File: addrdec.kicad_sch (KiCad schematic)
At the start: 4 parts, among them U10 74LS138, U11 74HCT00, U24 74LS32, U9 74LS27

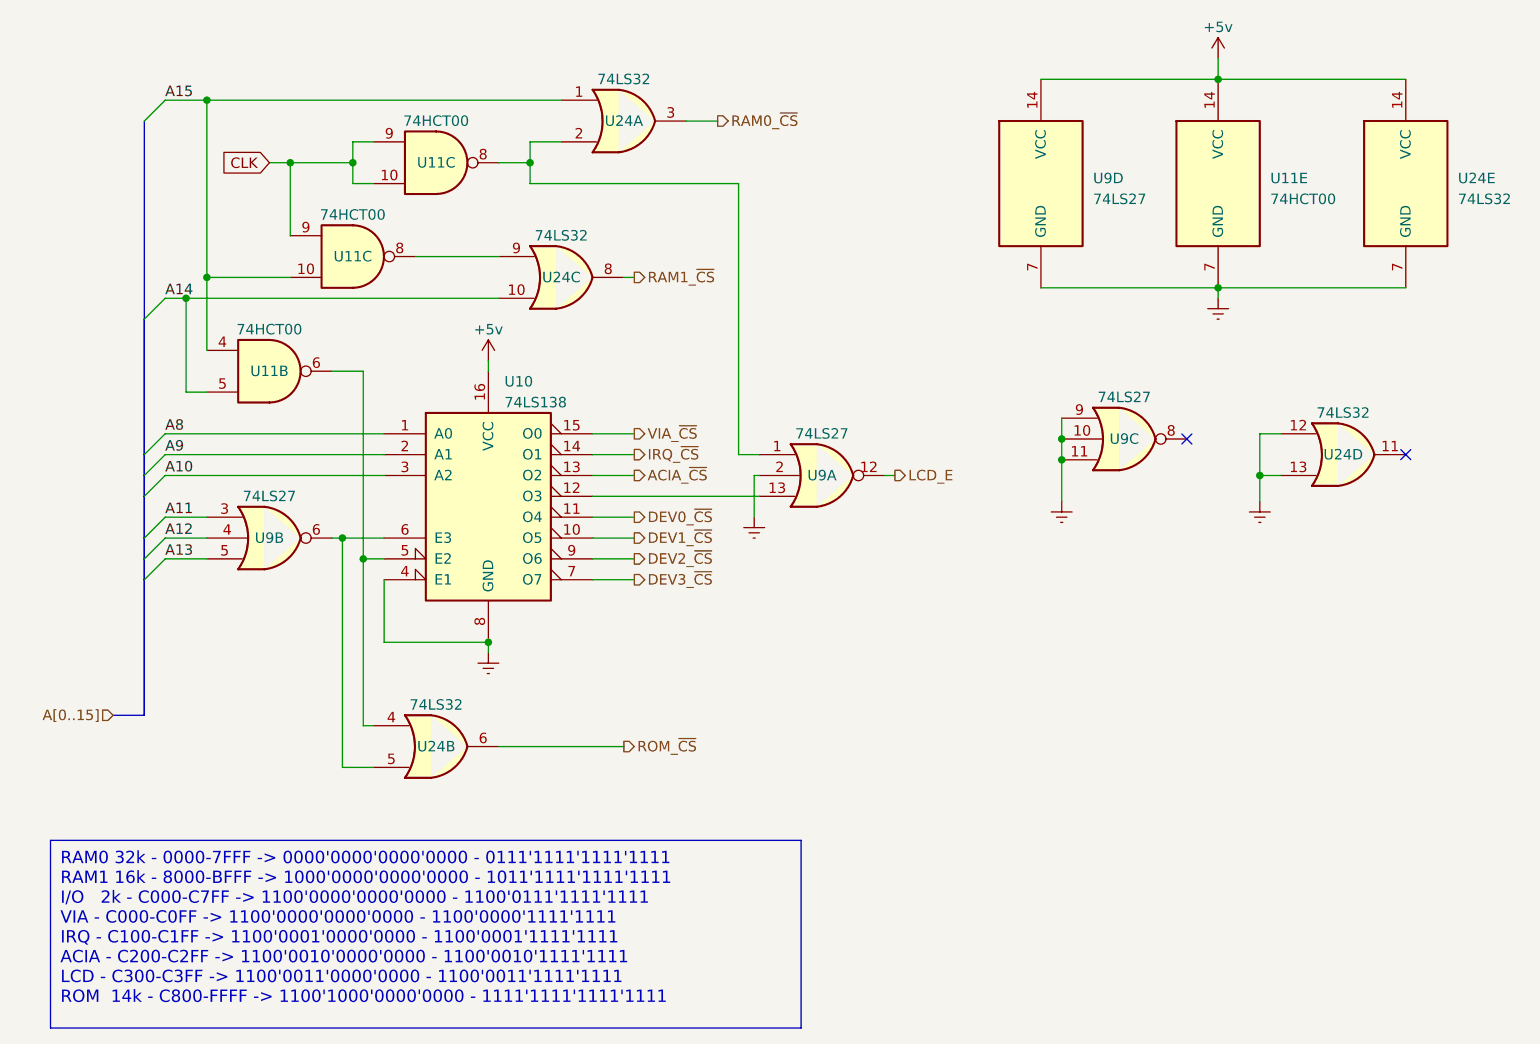
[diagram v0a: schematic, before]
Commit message: fix addrdec design bug, use ca65/cmake instead of vasm/make
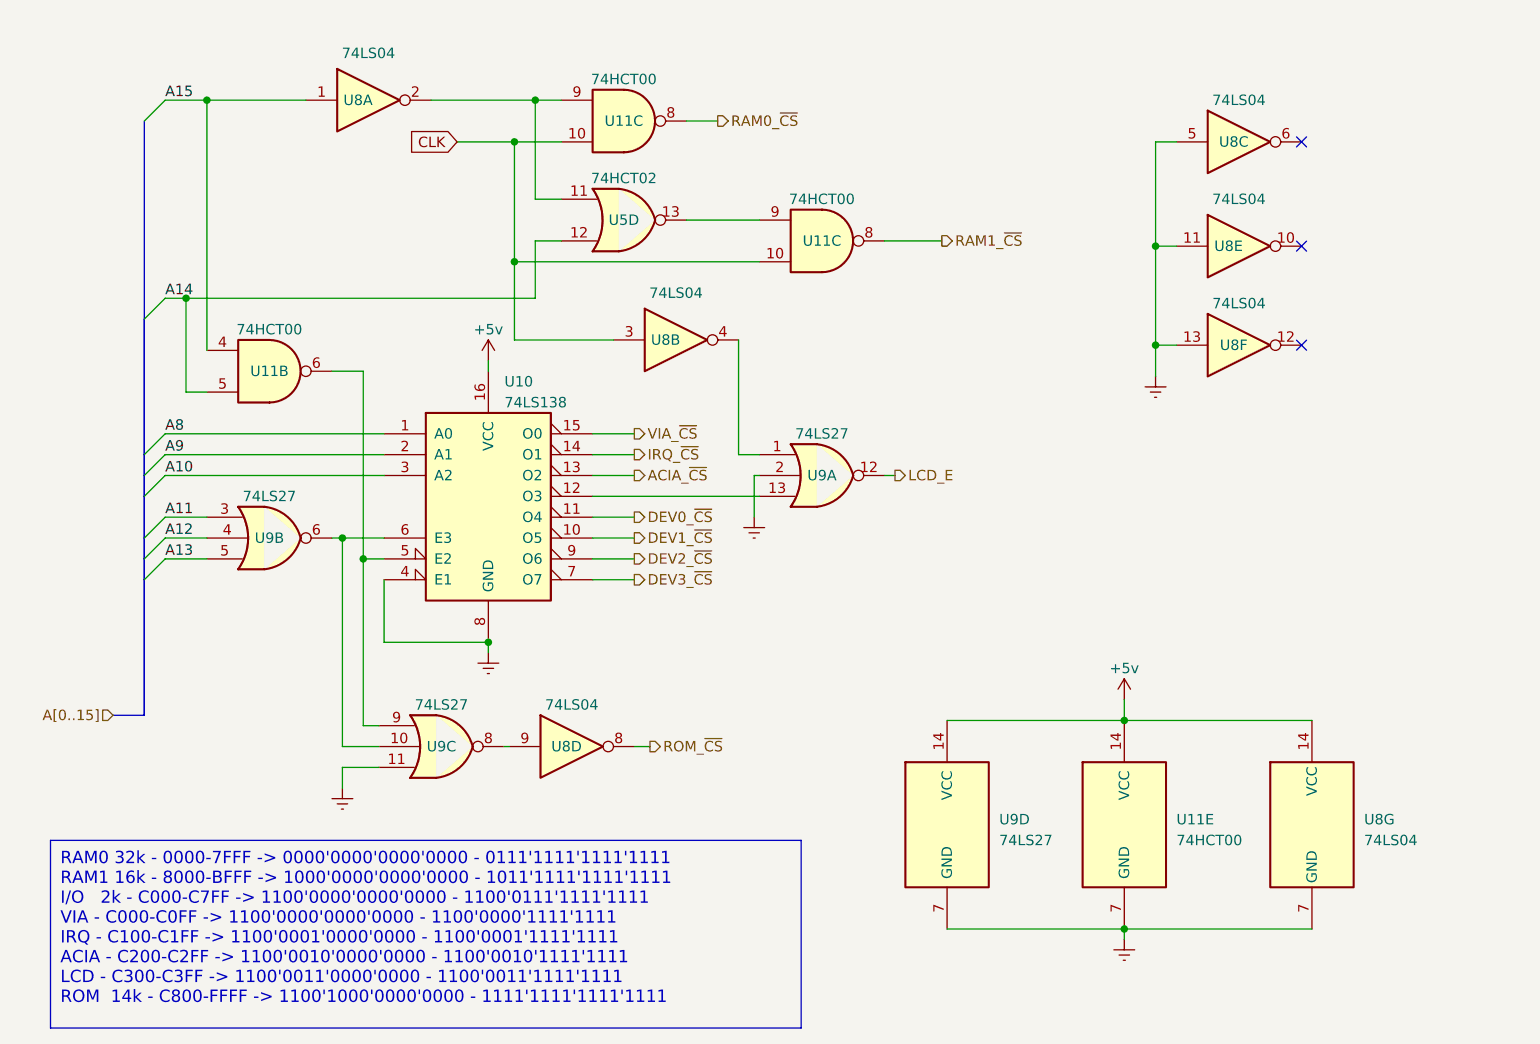
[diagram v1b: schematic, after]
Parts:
- removed U24: 74LS32, symbol 74xx:74LS32
- added U5: 74HCT02, symbol 74xx:74HCT02
- added U8: 74LS04, symbol 74xx:74LS04
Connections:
- net A14: now also U5.12
- net A15: now also U8.1; no longer U11.10
- net CLK: now also U11.10, U8.3; no longer U11.9, U11.9
- net Earth: now also U8.11, U8.13, U8.5, U8.7 (GND); no longer U9.10, U9.9
- net RAM0_~{CS}: now also U11.8
- net RAM1_~{CS}: now also U11.8
- net ROM_~{CS}: now also U8.8
- net VCC: now also U8.14 (VCC)
- net at U10.6 (E3), U9.6: now also U9.10
- net at U9.8: now also U8.9
- net at U9.1: now also U8.4; no longer U11.8
- net at U10.5 (E2), U11.6: now also U9.9
- new net: U11.9, U5.11, U8.2
- new net: U11.9, U5.13
- no-connect marks 2 -> 3
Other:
- moved on the sheet: U11C, U11E, U9C, U9D

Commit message: add address decoding timings
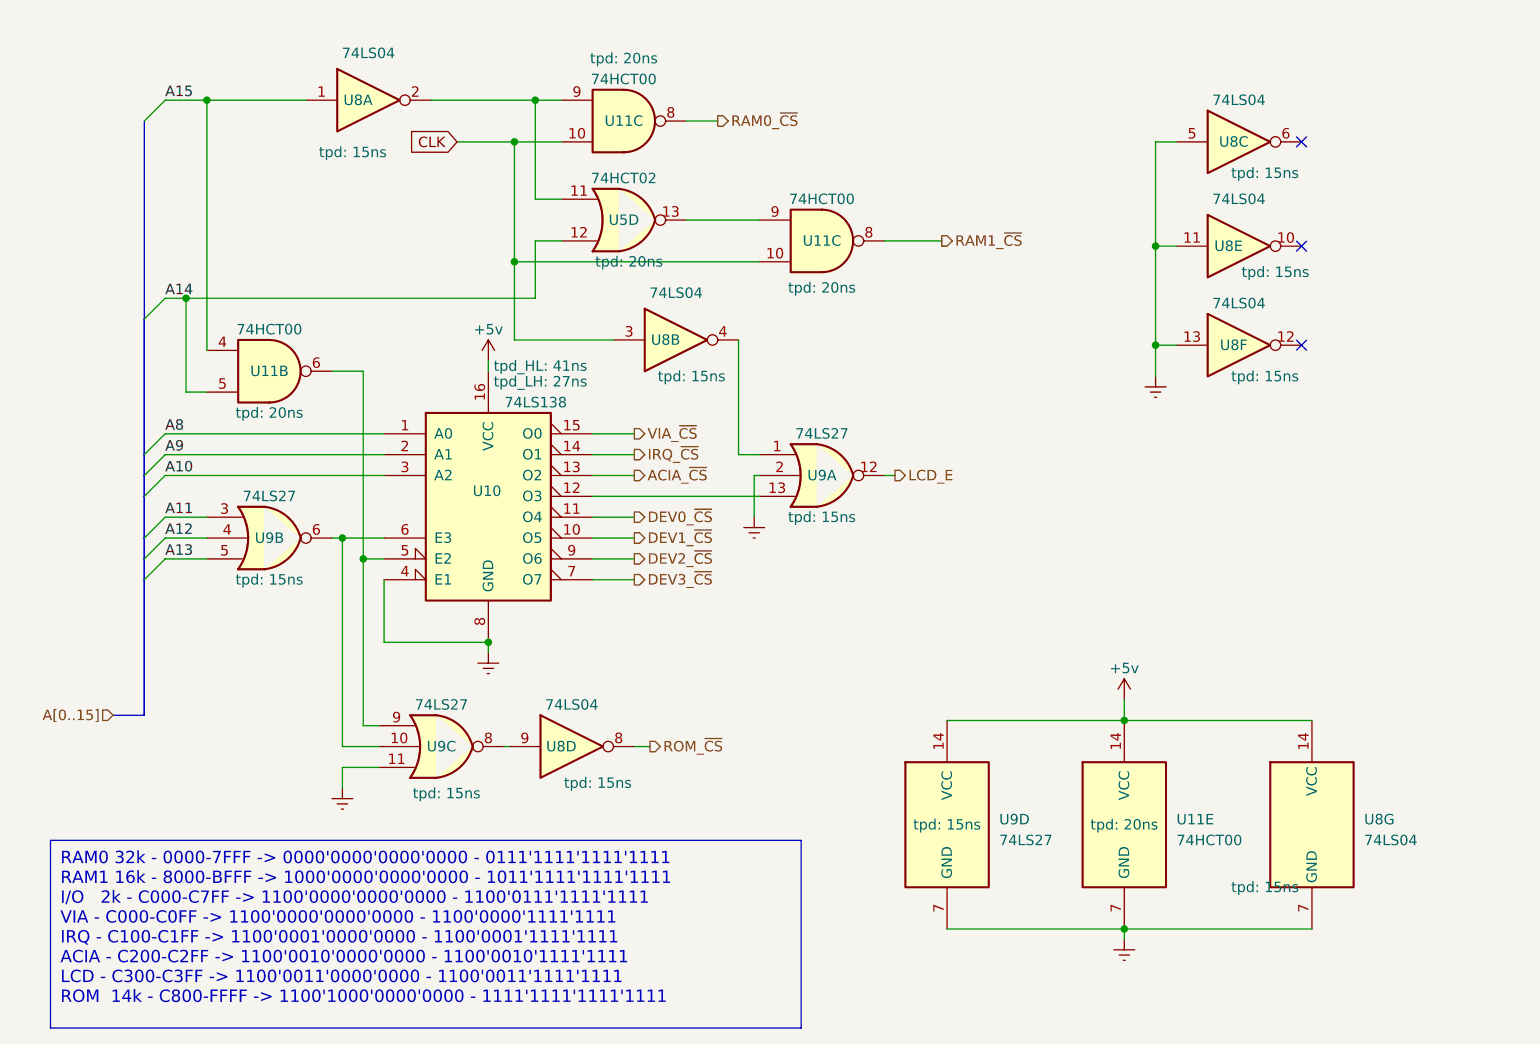
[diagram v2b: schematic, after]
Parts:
- U10: tpd_HL (none) -> 41ns; tpd_LH (none) -> 27ns
- U11, U5: tpd (none) -> 20ns
- U8, U9: tpd (none) -> 15ns
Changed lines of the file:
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@@
     (effects (font (size 1.27 1.27)) (justify left))
   )
-  (hierarchical_label "RAM1_~{CS}" (shape output) (at 125.095 41.275 0) (fields_autoplaced)
+  (hierarchical_label "RAM1_~{CS}" (shape output) (at 125.095 41.275 0)
     (effects (font (size 1.27 1.27)) (justify left))
+    (property "tpd_HL" "55ns" (at 121.285 46.355 0) (show_name)
+      (effects (font (size 1.27 1.27) italic) (justify left))
+    )
+    (property "tpd_LH" "20ns" (at 121.285 43.815 0) (show_name)
+      (effects (font (size 1.27 1.27) italic) (justify left))
+    )
   )
   (hierarchical_label "A[0..15]" (shape input) (at 24.13 99.06 180) (fields_autoplaced)
@@
     (effects (font (size 1.27 1.27)) (justify left))
   )
-  (hierarchical_label "ROM_~{CS}" (shape output) (at 89.535 102.87 0) (fields_autoplaced)
+  (hierarchical_label "ROM_~{CS}" (shape output) (at 89.535 102.87 0)
     (effects (font (size 1.27 1.27)) (justify left))
+    (property "tpd" "50ns" (at 89.535 104.775 0) (show_name)
+      (effects (font (size 1.27 1.27) italic) (justify left))
+    )
   )
   (hierarchical_label "IRQ_~{CS}" (shape output) (at 87.63 67.31 0) (fields_autoplaced)
@@
     (effects (font (size 1.27 1.27)) (justify left))
   )
-  (hierarchical_label "RAM0_~{CS}" (shape output) (at 97.79 26.67 0) (fields_autoplaced)
+  (hierarchical_label "RAM0_~{CS}" (shape output) (at 97.79 26.67 0)
     (effects (font (size 1.27 1.27)) (justify left))
+    (property "tpd_LH" "15ns" (at 95.25 29.21 0) (show_name)
+      (effects (font (size 1.27 1.27) italic) (justify left))
+    )
+    (property "tpd_HL" "35ns" (at 100.965 31.115 0) (show_name)
+      (effects (font (size 1.27 1.27) italic))
+    )
   )
   (symbol (lib_id "74xx:74LS27") (at 43.18 77.47 0) (unit 2)
@@
       (effects (font (size 1.27 1.27)) hide)
     )
+    (property "tpd" "15ns" (at 43.18 82.55 0) (show_name)
+      (effects (font (size 1.27 1.27)))
+    )
     (pin "1")
     (pin "12")
@@
     (property "Datasheet" "http://www.ti.com/lit/gpn/sn74hct02" (at 86.36 38.735 0)
       (effects (font (size 1.27 1.27)) hide)
+    )
+    (property "tpd" "20ns" (at 86.995 43.815 0) (show_name)
+      (effects (font (size 1.27 1.27)))
     )
     (pin "1")
@@
       (effects (font (size 1.27 1.27)) hide)
     )
+    (property "tpd" "15ns" (at 64.77 108.585 0) (show_name)
+      (effects (font (size 1.27 1.27)))
+    )
     (pin "1")
     (pin "12")
@@
     (property "Datasheet" "http://www.ti.com/lit/gpn/sn74hct00" (at 86.36 26.67 0)
       (effects (font (size 1.27 1.27)) hide)
+    )
+    (property "tpd" "20ns" (at 86.36 19.05 0) (show_name)
+      (effects (font (size 1.27 1.27)))
     )
     (pin "1")
@@
       (effects (font (size 1.27 1.27)) hide)
     )
+    (property "tpd" "15ns" (at 125.73 112.395 0) (show_name)
+      (effects (font (size 1.27 1.27)))
+    )
     (pin "1")
     (pin "12")
@@
       (effects (font (size 1.27 1.27)) hide)
     )
+    (property "tpd" "15ns" (at 164.465 120.015 0) (show_name)
+      (effects (font (size 1.27 1.27)))
+    )
     (pin "1")
     (pin "2")
@@
   )
   (symbol (lib_id "74xx:74LS138") (at 69.85 72.39 0) (unit 1)
-    (in_bom yes) (on_board yes) (dnp no) (fields_autoplaced)
-    (property "Reference" "U10" (at 71.8059 58.42 0)
+    (in_bom yes) (on_board yes) (dnp no)
+    (property "Reference" "U10" (at 67.945 71.755 0)
       (effects (font (size 1.27 1.27)) (justify left))
     )
@@
       (effects (font (size 1.27 1.27)) hide)
     )
+    (property "tpd_HL" "41ns" (at 76.2 56.515 0) (show_name)
+      (effects (font (size 1.27 1.27)))
+    )
+    (property "tpd_LH" "27ns" (at 76.2 58.42 0) (show_name)
+      (effects (font (size 1.27 1.27)))
+    )
     (pin "1")
     (pin "10")
@@
       (effects (font (size 1.27 1.27)) hide)
     )
+    (property "tpd" "20ns" (at 147.32 112.395 0) (show_name)
+      (effects (font (size 1.27 1.27)))
+    )
     (pin "1")
     (pin "2")
@@
     (property "Datasheet" "http://www.ti.com/lit/gpn/sn74LS27" (at 110.49 69.85 0)
       (effects (font (size 1.27 1.27)) hide)
+    )
+    (property "tpd" "15ns" (at 110.49 74.93 0) (show_name)
+      (effects (font (size 1.27 1.27)))
     )
     (pin "1")
@@
       (effects (font (size 1.27 1.27)) hide)
     )
+    (property "tpd" "15ns" (at 165.735 45.085 0) (show_name)
+      (effects (font (size 1.27 1.27)))
+    )
     (pin "1")
     (pin "2")
@@
     (property "Datasheet" "http://www.ti.com/lit/gpn/sn74LS04" (at 55.245 24.13 0)
       (effects (font (size 1.27 1.27)) hide)
+    )
+    (property "tpd" "15ns" (at 53.34 30.48 0) (show_name)
+      (effects (font (size 1.27 1.27)))
     )
     (pin "1")
@@
       (effects (font (size 1.27 1.27)) hide)
     )
+    (property "tpd" "15ns" (at 164.465 57.785 0) (show_name)
+      (effects (font (size 1.27 1.27)))
+    )
     (pin "1")
     (pin "2")
@@
       (effects (font (size 1.27 1.27)) hide)
     )
+    (property "tpd" "20ns" (at 43.18 62.23 0) (show_name)
+      (effects (font (size 1.27 1.27)))
+    )
     (pin "1")
     (pin "2")
@@
       (effects (font (size 1.27 1.27)) hide)
     )
+    (property "tpd" "15ns" (at 94.615 57.785 0) (show_name)
+      (effects (font (size 1.27 1.27)))
+    )
     (pin "1")
     (pin "2")
@@
     (property "Datasheet" "http://www.ti.com/lit/gpn/sn74hct00" (at 110.49 41.275 0)
       (effects (font (size 1.27 1.27)) hide)
+    )
+    (property "tpd" "20ns" (at 110.49 46.99 0) (show_name)
+      (effects (font (size 1.27 1.27)))
     )
     (pin "1")
@@
       (effects (font (size 1.27 1.27)) hide)
     )
+    (property "tpd" "15ns" (at 164.465 33.02 0) (show_name)
+      (effects (font (size 1.27 1.27)))
+    )
     (pin "1")
     (pin "2")
@@
   (symbol (lib_id "74xx:74LS04") (at 80.01 102.87 0) (unit 4)
     (in_bom yes) (on_board yes) (dnp no)
-    (property "Reference" "U8" (at 79.375 102.87 0)
+    (property "Reference" "U8" (at 78.74 102.87 0)
       (effects (font (size 1.27 1.27)))
     )
@@
       (effects (font (size 1.27 1.27)) hide)
     )
-    (pin "1")
+    (property "tpd" "15ns" (at 83.185 107.315 0) (show_name)
+      (effects (font (size 1.27 1.27)))
+    )
+    (pin "1")
